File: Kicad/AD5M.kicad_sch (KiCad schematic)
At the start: 20 parts, among them J1 Vin, J2 Conn_01x11, J3 Ext, M1 4020, M2 5015, U1 LMR14006Y, U2 ESP32 C3 SuperMini, U3 BME280 Module, U4 ENS160 Module, U5 DRV8871 Module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

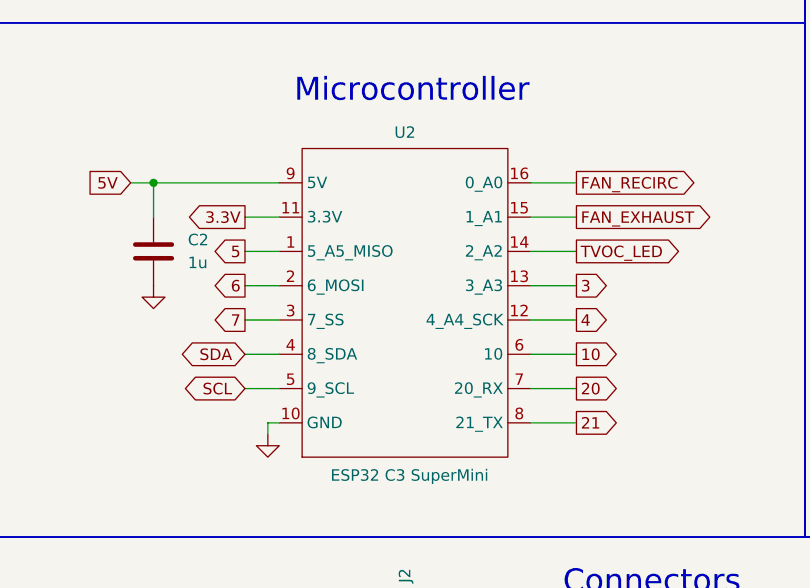
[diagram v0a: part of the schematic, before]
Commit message: Fixed ESP32 footprint & symbol Updated KiCad files Updated gerbers to board version 1.1
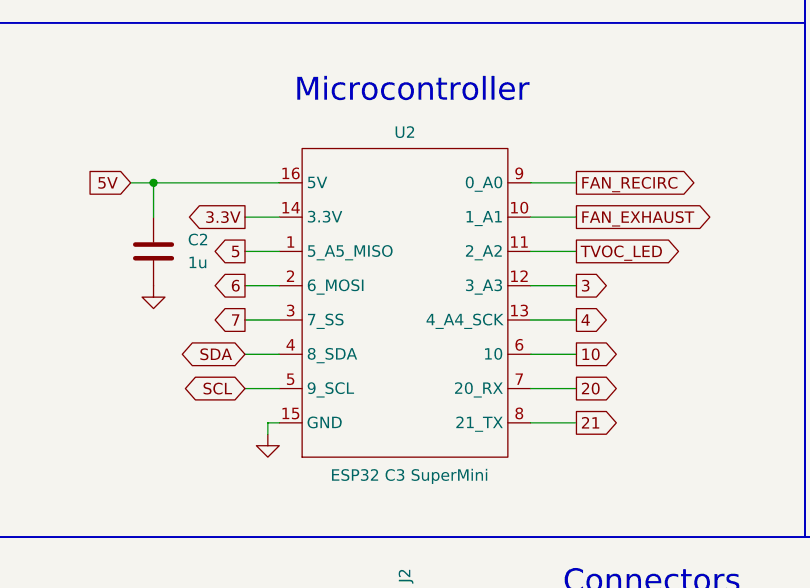
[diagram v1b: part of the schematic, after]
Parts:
- D1: footprint Diode_SMD:D_SOD-123 -> Diode_SMD:D_SOD-323
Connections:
- net 3: now also U2.12 (3_A3); no longer U2.13 (3_A3)
- net 3.3V: now also U2.14 (3.3V); no longer U2.11 (3.3V)
- net 4: now also U2.13 (4_A4_SCK); no longer U2.12 (4_A4_SCK)
- net 5V: now also U2.16 (5V); no longer U2.9 (5V)
- net FAN_EXHAUST: now also U2.10 (1_A1); no longer U2.15 (1_A1)
- net FAN_RECIRC: now also U2.9 (0_A0); no longer U2.16 (0_A0)
- net GND: now also U2.15 (GND); no longer U2.10 (GND)
- net TVOC_LED: now also U2.11 (2_A2); no longer U2.14 (2_A2)
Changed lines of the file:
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@@
 			)
 		)
-		(property "Datasheet" "https://www.lcsc.com/datasheet/C135271.pdf"
+		(property "Datasheet" "~"
 			(at 96.52 39.37 0)
 			(effects
@@
 			)
 		)
-		(property "Description" "Shun Xiang Nuo SMNR4030-6R8MT"
+		(property "Description" "Inductor"
 			(at 96.52 39.37 0)
 			(effects
@@
 			)
 		)
-		(property "Footprint" "Diode_SMD:D_SOD-123"
+		(property "Footprint" "Diode_SMD:D_SOD-323"
 			(at 80.645 44.45 0)
 			(effects
@@
 			)
 		)
-		(property "Datasheet" "https://www.lcsc.com/datasheet/C82544.pdf"
+		(property "Datasheet" "https://datasheet.lcsc.com/lcsc/2204281430_Guangdong-Hottech-1N5819WS_C191023.pdf"
 			(at 85.09 44.45 0)
 			(effects
@@
 	)
 	(symbol
-		(lib_name "DRV8871_Module_1")
 		(lib_id "Chryseus:DRV8871_Module")
 		(at 217.17 63.5 0)
